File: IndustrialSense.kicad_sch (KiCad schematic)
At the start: 0 parts

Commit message: First draft of the schematic
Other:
- removed sheet Power - Sequencing
- title: (none) -> MCU
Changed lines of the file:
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@@
 	(paper "A3")
 	(title_block
+		(title "MCU")
 		(date "2025-01-12")
 		(rev "${REVISION}")
@@
 			(type dot)
 			(color 0 0 0 1)
-		)
-	)
-	(sheet
-		(at 340.36 313.69)
-		(size 35.56 5.08)
-		(exclude_from_sim no)
-		(in_bom yes)
-		(on_board yes)
-		(dnp no)
-		(stroke
-			(width 0.1524)
-			(type solid)
-		)
-		(fill
-			(color 0 0 0 0.0000)
-		)
-		(property "Sheetname" "Power - Sequencing"
-			(at 340.36 312.6609 0)
-			(effects
-				(font
-					(face "Times New Roman")
-					(size 1.905 1.905)
-					(bold yes)
-					(color 0 0 0 1)
-				)
-				(justify left bottom)
-			)
-		)
-		(property "Sheetfile" "Power - Sequencing.kicad_sch"
-			(at 341.63 314.96 0)
-			(effects
-				(font
-					(face "Arial")
-					(size 1.27 1.27)
-				)
-				(justify left top)
-			)
-		)
-		(instances
-			(project "IndustrialSense"
-				(path "/f9e05184-c88b-4a88-ae9c-ab2bdb32be7c"
-					(page "6")
-				)
-			)
 		)
 	)
@@
 			(project "IndustrialSense"
 				(path "/f9e05184-c88b-4a88-ae9c-ab2bdb32be7c"
-					(page "7")
+					(page "10")
 				)
 			)

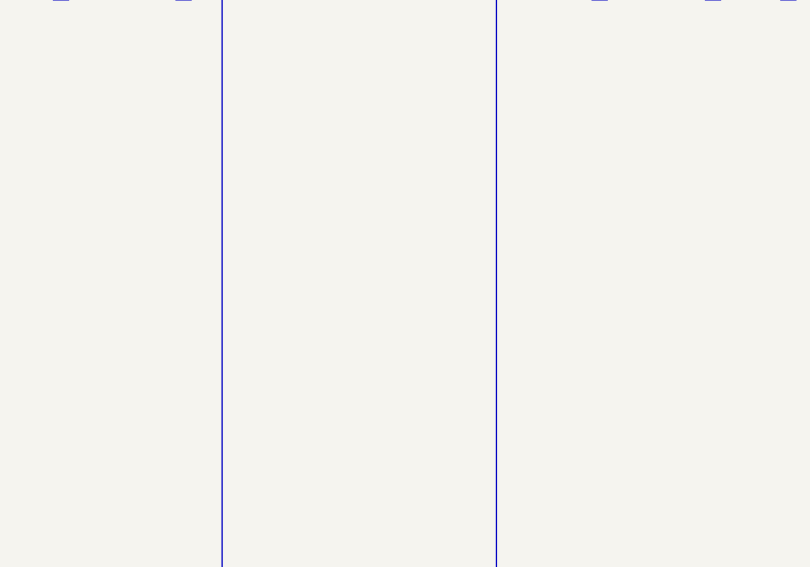
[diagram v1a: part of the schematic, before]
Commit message: [Schematic][Added] Project Architecture, connectors
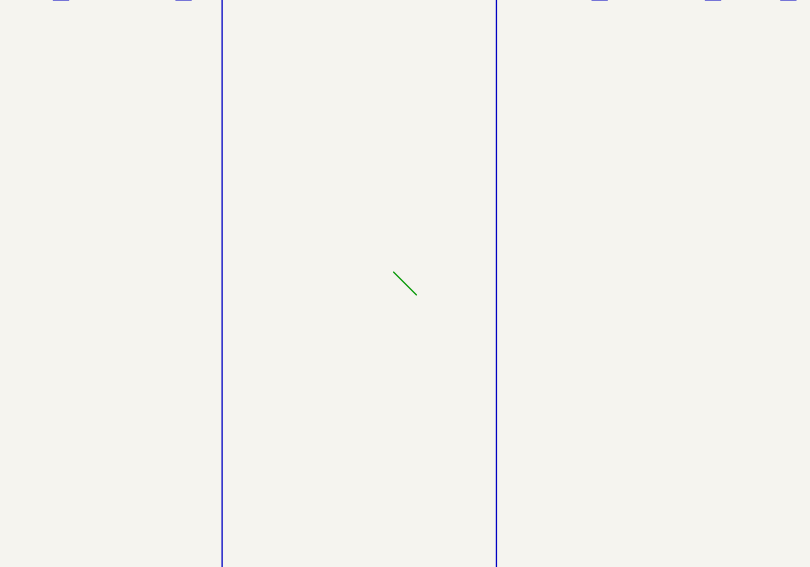
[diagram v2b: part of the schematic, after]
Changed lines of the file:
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@@
+		)
+	)
+	(bus_entry
+		(at 111.76 201.93)
+		(size 2.54 2.54)
+		(stroke
+			(width 0)
+			(type default)
 		)
 	)
@@
 			(project "IndustrialSense"
 				(path "/f9e05184-c88b-4a88-ae9c-ab2bdb32be7c"
-					(page "10")
+					(page "11")
 				)
 			)

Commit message: [PCB/SCH][Added] Preliminary version
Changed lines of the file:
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@@
-		)
-	)
-	(bus_entry
-		(at 111.76 201.93)
-		(size 2.54 2.54)
-		(stroke
-			(width 0)
-			(type default)
 		)
 	)

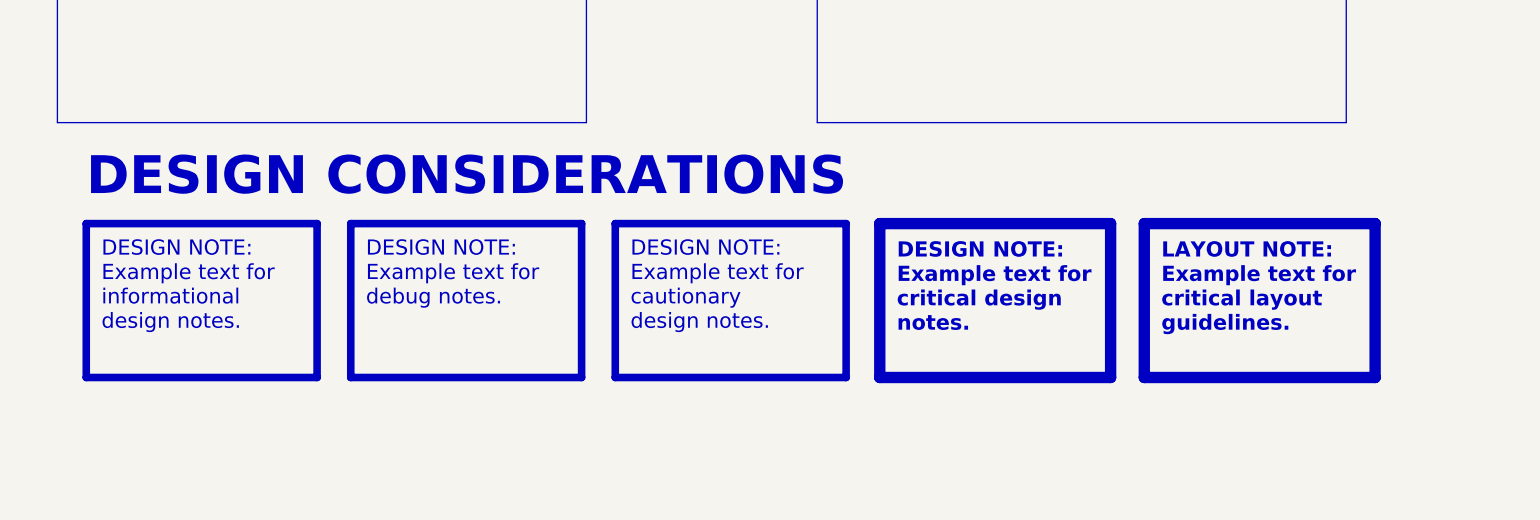
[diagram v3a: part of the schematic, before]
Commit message: [Schematic/PCB][Added] Routing finished, DRC finished
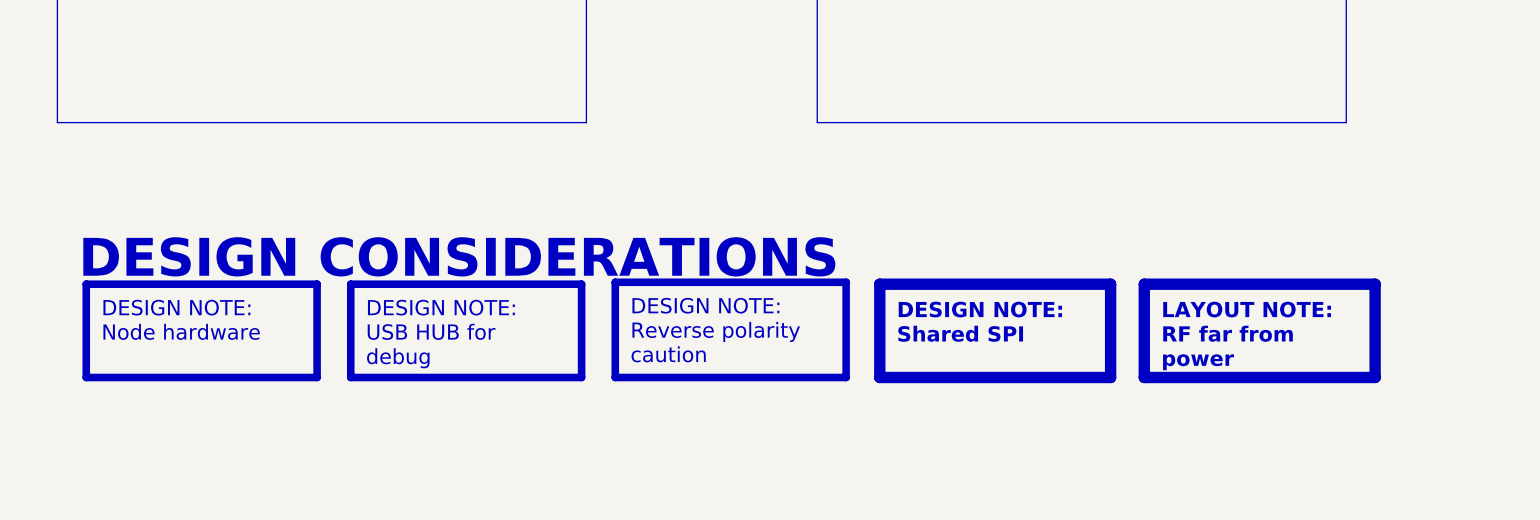
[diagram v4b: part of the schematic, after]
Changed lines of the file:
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@@
 	(text "DESIGN CONSIDERATIONS"
 		(exclude_from_sim no)
-		(at 26.67 255.27 0)
+		(at 25.654 266.192 0)
 		(effects
 			(font
@@
 		)
 	)
-	(text_box "DESIGN NOTE:\nExample text for cautionary design notes."
+	(text_box "DESIGN NOTE:\nReverse polarity caution"
 		(exclude_from_sim no)
-		(at 96.52 258.445 0)
-		(size 30.48 20.32)
+		(at 96.52 266.192 0)
+		(size 30.48 12.573)
 		(margins 2 2 2 2)
 		(stroke
@@
 		)
 	)
-	(text_box "DESIGN NOTE:\nExample text for debug notes."
+	(text_box "DESIGN NOTE:\nUSB HUB for debug"
 		(exclude_from_sim no)
-		(at 61.595 258.445 0)
-		(size 30.48 20.32)
+		(at 61.595 266.446 0)
+		(size 30.48 12.319)
 		(margins 2 2 2 2)
 		(stroke
@@
 		)
 	)
-	(text_box "DESIGN NOTE:\nExample text for critical design notes."
+	(text_box "DESIGN NOTE:\nShared SPI"
 		(exclude_from_sim no)
-		(at 131.445 258.445 0)
-		(size 30.48 20.32)
+		(at 131.445 266.446 0)
+		(size 30.48 12.319)
 		(margins 2.25 2.25 2.25 2.25)
 		(stroke
@@
 		)
 	)
-	(text_box "LAYOUT NOTE:\nExample text for critical layout guidelines."
+	(text_box "LAYOUT NOTE:\nRF far from power\n"
 		(exclude_from_sim no)
-		(at 166.37 258.445 0)
-		(size 30.48 20.32)
+		(at 166.37 266.446 0)
+		(size 30.48 12.319)
 		(margins 2.25 2.25 2.25 2.25)
 		(stroke
@@
 		)
 	)
-	(text_box "DESIGN NOTE:\nExample text for informational design notes."
+	(text_box "DESIGN NOTE:\nNode hardware"
 		(exclude_from_sim no)
-		(at 26.67 258.445 0)
-		(size 30.48 20.32)
+		(at 26.67 266.446 0)
+		(size 30.48 12.319)
 		(margins 2 2 2 2)
 		(stroke

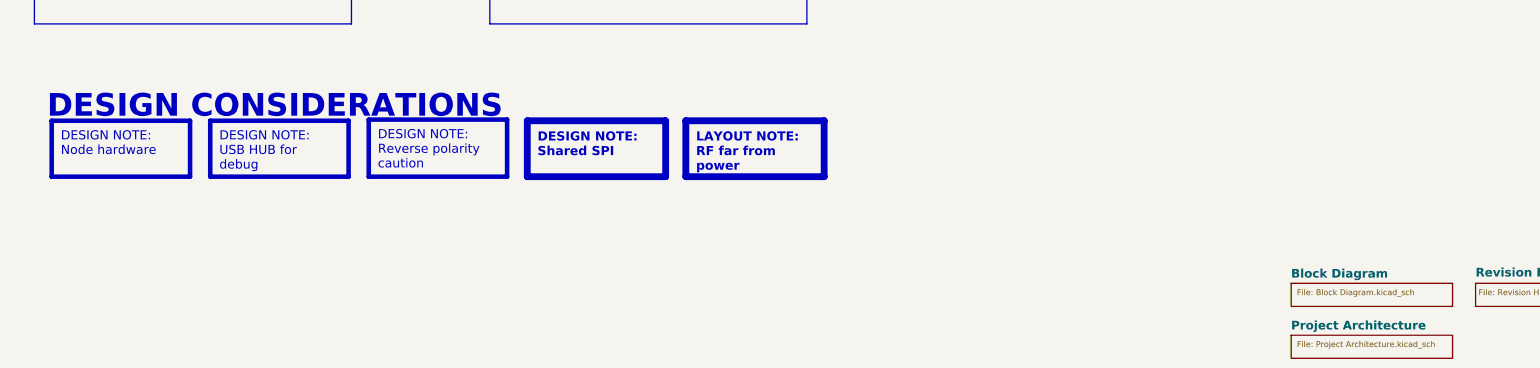
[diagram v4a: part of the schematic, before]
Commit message: [Schematic/PCB][Added] Testpoints and fabrication files test
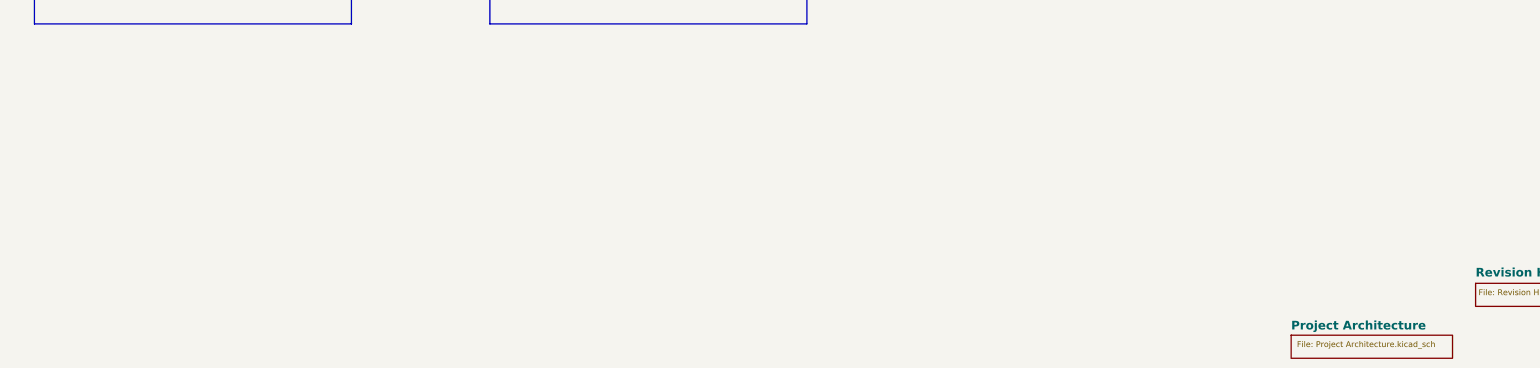
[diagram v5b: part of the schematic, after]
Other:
- removed sheet Block Diagram
- note removed: "DESIGN CONSIDERATIONS"
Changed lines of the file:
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@@
-		)
-	)
-	(text "DESIGN CONSIDERATIONS"
-		(exclude_from_sim no)
-		(at 25.654 266.192 0)
-		(effects
-			(font
-				(face "Arial")
-				(size 5 5)
-				(bold yes)
-				(color 53 60 207 1)
-			)
-			(justify left bottom)
-		)
-	)
-	(text_box "DESIGN NOTE:\nReverse polarity caution"
-		(exclude_from_sim no)
-		(at 96.52 266.192 0)
-		(size 30.48 12.573)
-		(margins 2 2 2 2)
-		(stroke
-			(width 1)
-			(type solid)
-			(color 250 236 0 1)
-		)
-		(fill
-			(type none)
-		)
-		(effects
-			(font
-				(face "Arial")
-				(size 2 2)
-				(color 0 0 0 1)
-			)
-			(justify left top)
-		)
-	)
-	(text_box "DESIGN NOTE:\nUSB HUB for debug"
-		(exclude_from_sim no)
-		(at 61.595 266.446 0)
-		(size 30.48 12.319)
-		(margins 2 2 2 2)
-		(stroke
-			(width 1)
-			(type solid)
-			(color 255 165 0 1)
-		)
-		(fill
-			(type none)
-		)
-		(effects
-			(font
-				(face "Arial")
-				(size 2 2)
-				(color 0 0 0 1)
-			)
-			(justify left top)
-		)
-	)
-	(text_box "DESIGN NOTE:\nShared SPI"
-		(exclude_from_sim no)
-		(at 131.445 266.446 0)
-		(size 30.48 12.319)
-		(margins 2.25 2.25 2.25 2.25)
-		(stroke
-			(width 1.5)
-			(type solid)
-			(color 255 0 0 1)
-		)
-		(fill
-			(type none)
-		)
-		(effects
-			(font
-				(face "Arial")
-				(size 2 2)
-				(thickness 0.4)
-				(bold yes)
-				(color 255 0 0 1)
-			)
-			(justify left top)
-		)
-	)
-	(text_box "LAYOUT NOTE:\nRF far from power\n"
-		(exclude_from_sim no)
-		(at 166.37 266.446 0)
-		(size 30.48 12.319)
-		(margins 2.25 2.25 2.25 2.25)
-		(stroke
-			(width 1.5)
-			(type solid)
-			(color 0 0 255 1)
-		)
-		(fill
-			(type none)
-		)
-		(effects
-			(font
-				(face "Arial")
-				(size 2 2)
-				(thickness 0.4)
-				(bold yes)
-				(color 0 0 255 1)
-			)
-			(justify left top)
 		)
 	)
@@
 			(font
 				(size 2.54 2.54)
-			)
-			(justify left top)
-		)
-	)
-	(text_box "DESIGN NOTE:\nNode hardware"
-		(exclude_from_sim no)
-		(at 26.67 266.446 0)
-		(size 30.48 12.319)
-		(margins 2 2 2 2)
-		(stroke
-			(width 1)
-			(type solid)
-			(color 200 200 200 1)
-		)
-		(fill
-			(type none)
-		)
-		(effects
-			(font
-				(face "Arial")
-				(size 2 2)
-				(color 0 0 0 1)
 			)
 			(justify left top)
@@
 			(project "IndustrialSense"
 				(path "/f9e05184-c88b-4a88-ae9c-ab2bdb32be7c"
-					(page "11")
+					(page "10")
 				)
 			)
@@
 	)
 	(sheet
-		(at 299.72 302.26)
+		(at 299.72 313.69)
 		(size 35.56 5.08)
 		(exclude_from_sim no)
@@
 			(color 0 0 0 0.0000)
 		)
-		(property "Sheetname" "Block Diagram"
-			(at 299.72 301.2309 0)
+		(property "Sheetname" "Project Architecture"
+			(at 299.72 312.6609 0)
 			(effects
 				(font
@@
 			)
 		)
-		(property "Sheetfile" "Block Diagram.kicad_sch"
-			(at 300.99 303.53 0)
+		(property "Sheetfile" "Project Architecture.kicad_sch"
+			(at 300.99 314.96 0)
 			(effects
 				(font
@@
 				)
 			)
-		)
-	)
-	(sheet
-		(at 299.72 313.69)
-		(size 35.56 5.08)
-		(exclude_from_sim no)
-		(in_bom yes)
-		(on_board yes)
-		(dnp no)
-		(stroke
-			(width 0.1524)
-			(type solid)
-		)
-		(fill
-			(color 0 0 0 0.0000)
-		)
-		(property "Sheetname" "Project Architecture"
-			(at 299.72 312.6609 0)
-			(effects
-				(font
-					(face "Times New Roman")
-					(size 1.905 1.905)
-					(bold yes)
-					(color 0 0 0 1)
-				)
-				(justify left bottom)
-			)
-		)
-		(property "Sheetfile" "Project Architecture.kicad_sch"
-			(at 300.99 314.96 0)
-			(effects
-				(font
-					(face "Arial")
-					(size 1.27 1.27)
-				)
-				(justify left top)
-			)
-		)
-		(instances
-			(project "IndustrialSense"
-				(path "/f9e05184-c88b-4a88-ae9c-ab2bdb32be7c"
-					(page "3")
-				)
-			)
